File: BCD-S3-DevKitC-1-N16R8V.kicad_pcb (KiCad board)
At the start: 4 copper layers, 29 x 57 mm, 51 parts, among them J1 Conn_01x22, J2 Conn_01x22, Q1 SS8050, Q2 SS8050, SW1 BOOT, SW2 RESET, U1 ESP32-S3-WROOM-1, U2 AMS1117-3.3, U3 CH343P

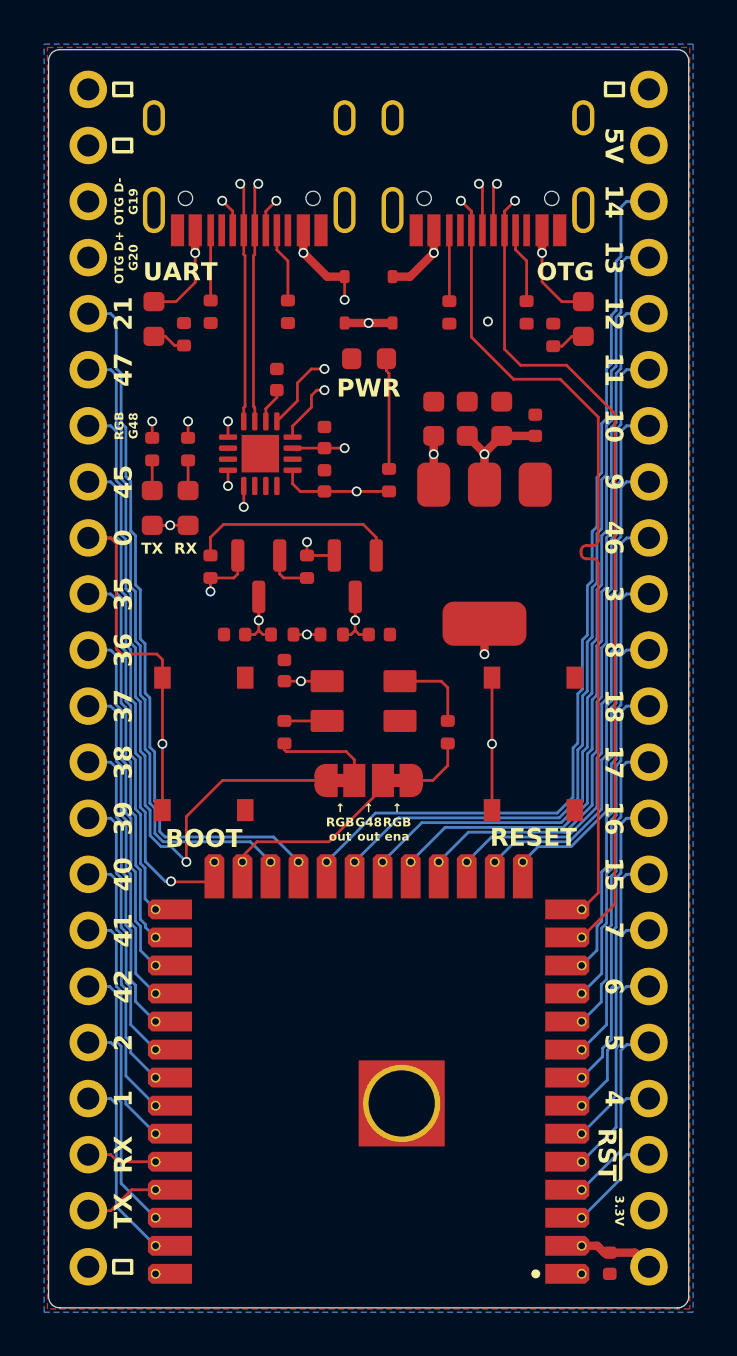
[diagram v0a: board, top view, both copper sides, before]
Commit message: Add help for RGB48 jumper. Fixed error in PCB for RGB48.
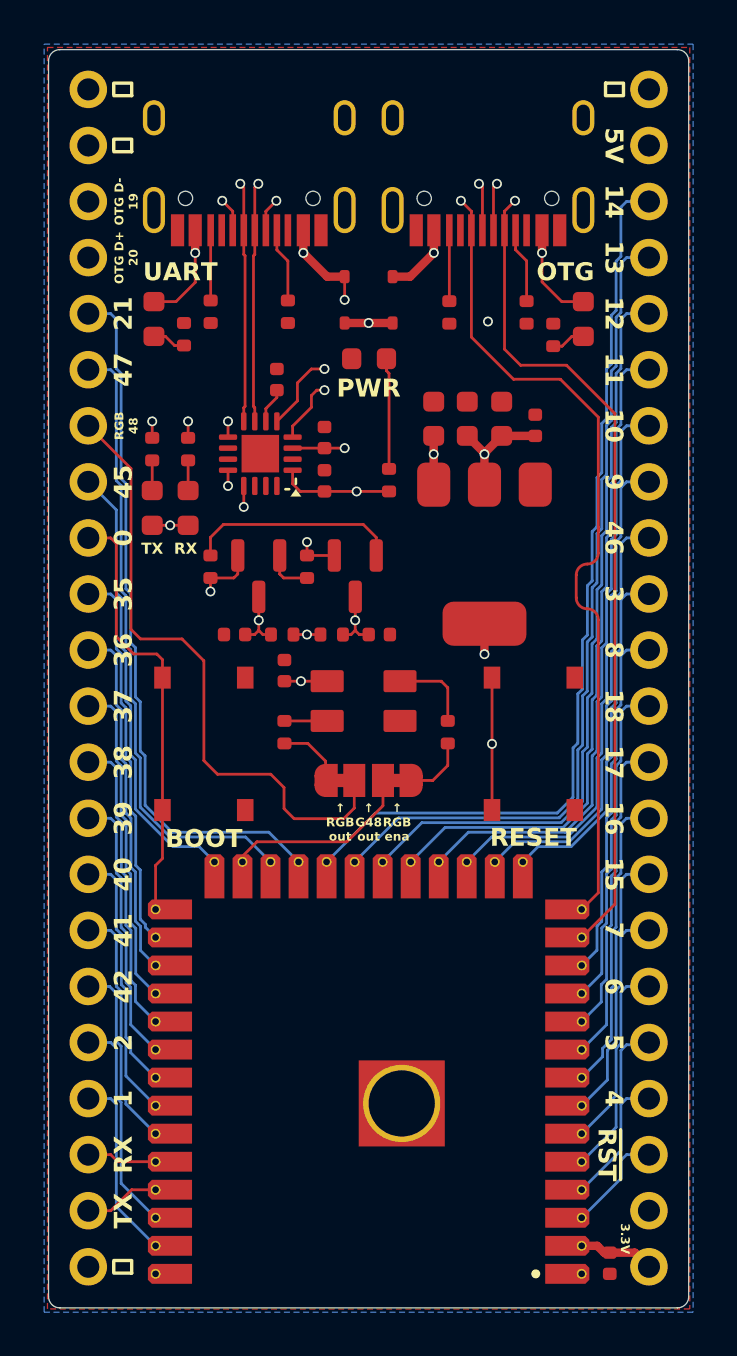
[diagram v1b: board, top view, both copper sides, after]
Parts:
- G2: footprint BeaupreCircuitDesign:BDC_QR_2.5mm -> BCD-S3-DevKitC-1-N16R8V:BCD-S3-DevKitC-1_5mm
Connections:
- JP3 pad 1: /RGB^{PIN} -> /RGB^{OUT}
- JP3 pad 2: /RGB^{OUT} -> /RGB^{PIN}
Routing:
- net /GPIO^{0}: track 44.5 -> 33.5 mm, vias 2 -> 1
- net /RGB^{PIN}: track 31.5 -> 28.4 mm, vias 1 -> 0
- net /GPIO^{45}: track 22.4 -> 20.3 mm, vias 1 -> 0
- net /RGB^{OUT}: track 4.58 -> 3.07 mm
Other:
- board text added: "OTG D+ 20"
- board text added: "OTG D- 19"
- board text added: "RGB 48"
- board text removed: "OTG D+ G20"
- board text removed: "OTG D- G19"
- board text removed: "RGB G48"
